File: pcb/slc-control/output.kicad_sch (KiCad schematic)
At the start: 4 parts, among them Q8 AO3400A, Q9 Q_Dual_PMOS_S1G1S2G2D2D2D1D1

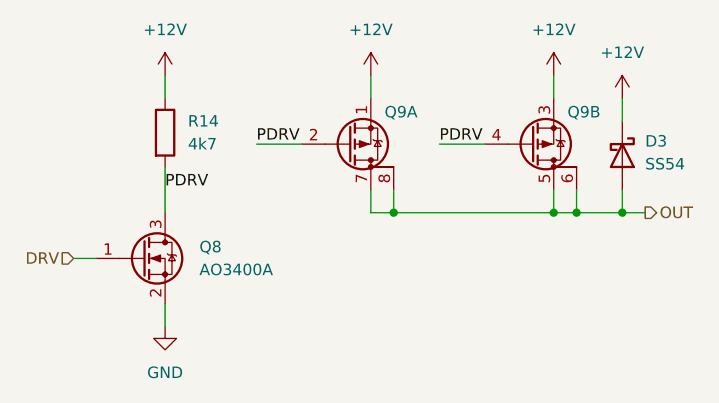
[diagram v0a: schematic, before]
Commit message: Change extended parts to do not place
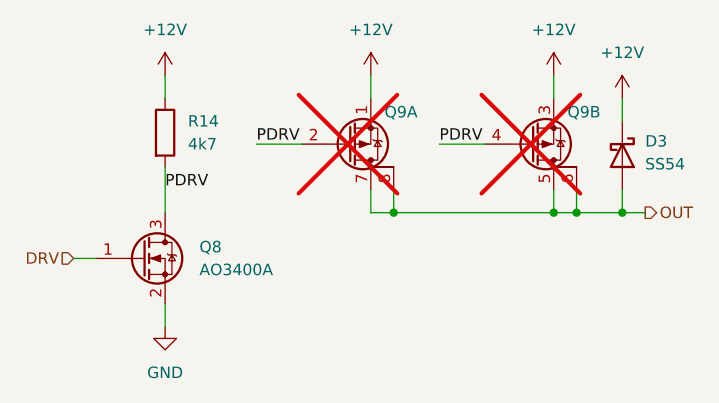
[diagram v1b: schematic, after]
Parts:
- Q9: now not fitted
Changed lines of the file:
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@@
 		(in_bom yes)
 		(on_board yes)
-		(dnp no)
+		(dnp yes)
 		(property "Reference" "Q9"
 			(at 80.264 63.754 0)
@@
 		(in_bom yes)
 		(on_board yes)
-		(dnp no)
+		(dnp yes)
 		(property "Reference" "Q9"
 			(at 100.584 63.754 0)
